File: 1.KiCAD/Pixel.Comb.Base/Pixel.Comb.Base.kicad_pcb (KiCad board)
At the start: 2 copper layers, 80 x 80 mm, 16 parts

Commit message: Added a second design of the Steel Vessel
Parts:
- removed the ? at (84.9, 81.6)
- removed the ? at (35.4, 81.6)
- removed the ? at (25.2, 56.8)
- removed the ? at (60.2, 91.8)
- removed the ? at (60.2, 21.8)
- removed the ? at (95.2, 56.8)
- removed the ? at (84.9, 32.1)
- removed the ? at (35.4, 32.1)
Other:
- outline, holes or cut-outs redrawn

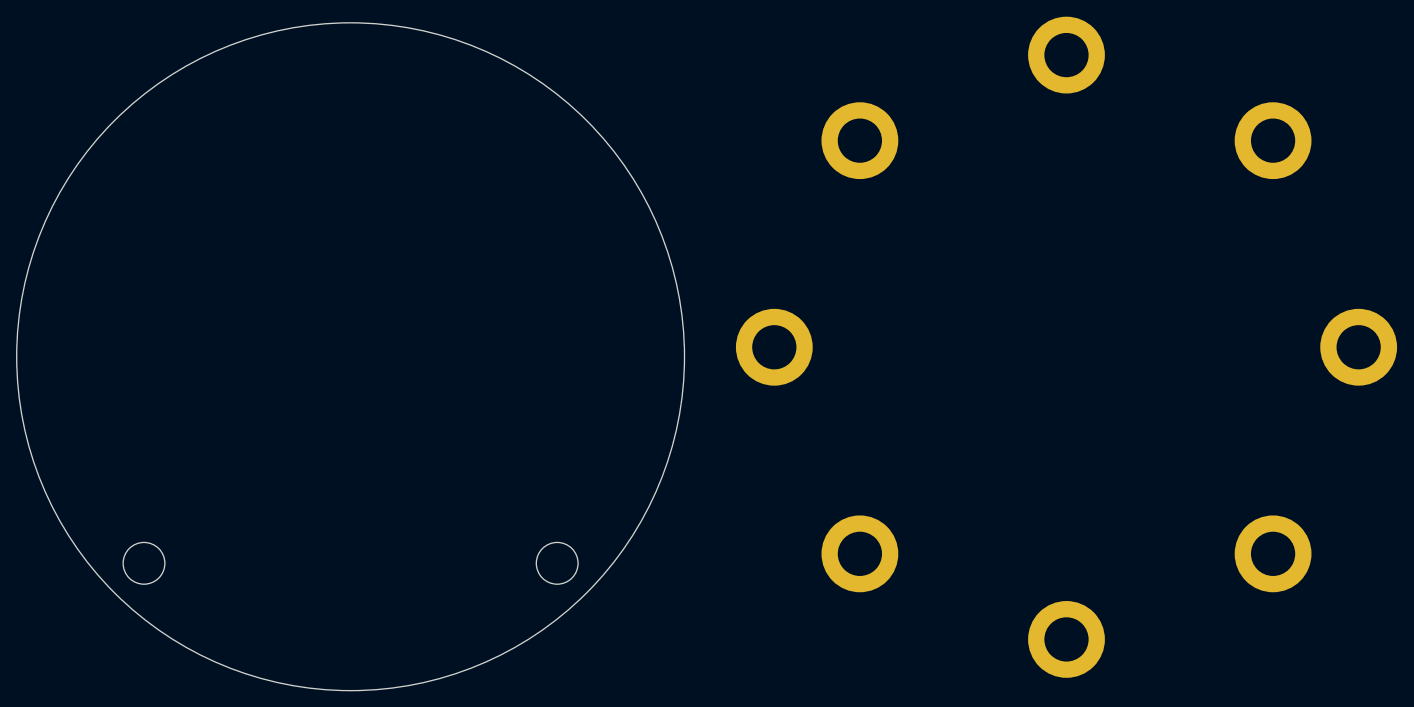
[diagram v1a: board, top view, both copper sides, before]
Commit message: Major changes to readout design
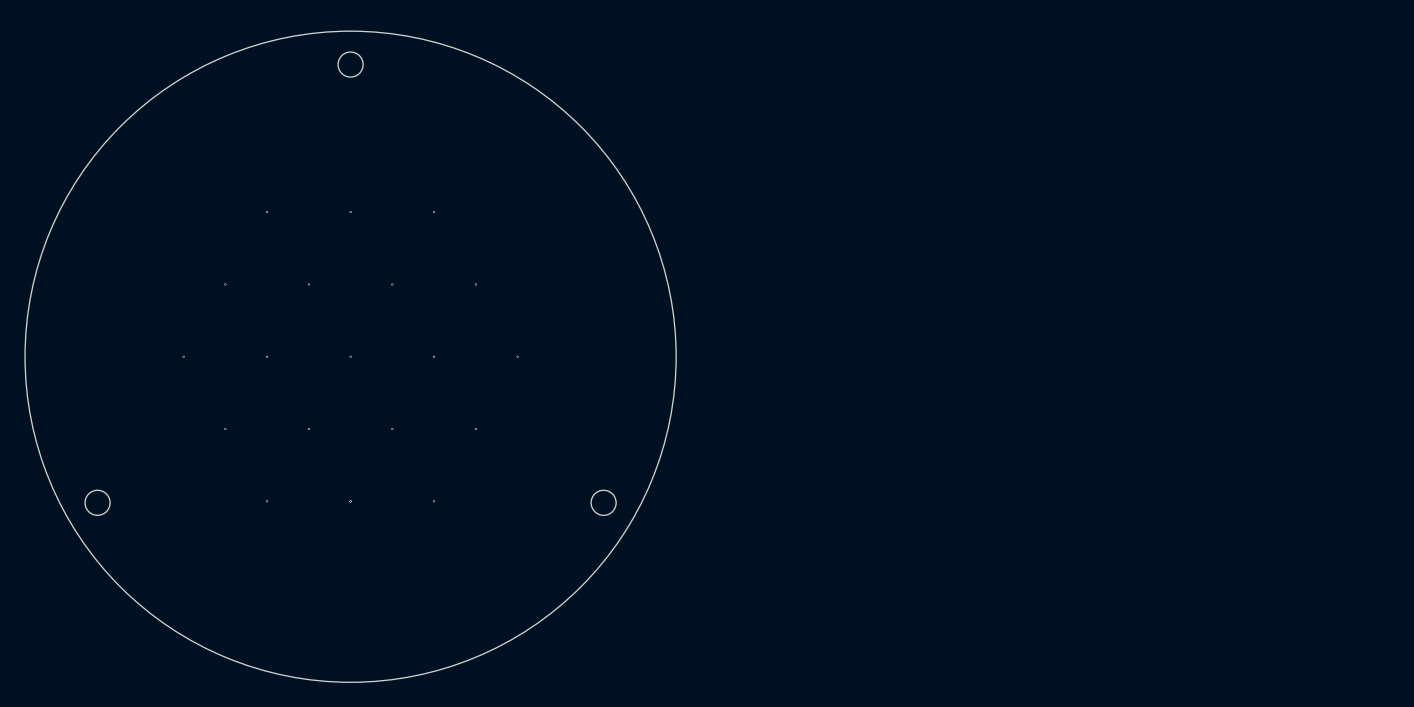
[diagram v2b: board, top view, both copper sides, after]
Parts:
- removed ? (x8): , 
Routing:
- net (no net): vias 0 -> 20
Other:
- board size 80 x 80 mm -> 78 x 78 mm
- board text added: "May 2023 Alfredo Barajas Enriquez"
